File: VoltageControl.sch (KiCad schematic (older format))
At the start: 7 parts

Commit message: Annotated sheets
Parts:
- gave numbers to parts that had none: 7
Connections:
- net at R201.1, RV201.3: now also U201.3 (+); no longer U201.5 (+)
- net at R202.2, R203.1: now also U201.2 (-); no longer U201.6 (-)
- net at D201.1 (K): now also U201.1; no longer U201.7
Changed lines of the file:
@@
 $EndDescr
 $Comp
-L LMV358 U?
-U 2 1 56A5F69C
+L LMV358 U201
+U 1 1 56A5F69C
 P 4250 4800
-F 0 "U?" H 4200 5000 60  0000 L CNN
+F 0 "U201" H 4200 5000 60  0000 L CNN
 F 1 "LMV358" H 4200 4550 60  0000 L CNN
 F 2 "" H 4250 4800 60  0000 C CNN
 F 3 "" H 4250 4800 60  0000 C CNN
-	2    4250 4800
+	1    4250 4800
 	1    0    0    -1
 $EndComp
 $Comp
-L R R?
+L R R201
 U 1 1 56A5F6A3
 P 2250 5750
-F 0 "R?" V 2330 5750 50  0000 C CNN
+F 0 "R201" V 2330 5750 50  0000 C CNN
 F 1 "R" V 2250 5750 50  0000 C CNN
 F 2 "" V 2180 5750 50  0000 C CNN
@@
 $EndComp
 $Comp
-L GND #PWR?
+L GND #PWR202
 U 1 1 56A5F6AA
 P 4150 5300
-F 0 "#PWR?" H 4150 5050 50  0001 C CNN
+F 0 "#PWR202" H 4150 5050 50  0001 C CNN
 F 1 "GND" H 4150 5150 50  0000 C CNN
 F 2 "" H 4150 5300 60  0000 C CNN
@@
 $EndComp
 $Comp
-L POT RV?
+L POT RV201
 U 1 1 56A5F6B0
 P 2250 4950
-F 0 "RV?" H 2250 4850 50  0000 C CNN
+F 0 "RV201" H 2250 4850 50  0000 C CNN
 F 1 "POT" H 2250 4950 50  0000 C CNN
 F 2 "" H 2250 4950 50  0000 C CNN
@@
 $EndComp
 $Comp
-L C C?
+L C C201
 U 1 1 56A5F6B7
 P 3450 4100
-F 0 "C?" H 3475 4200 50  0000 L CNN
+F 0 "C201" H 3475 4200 50  0000 L CNN
 F 1 "C" H 3475 4000 50  0000 L CNN
 F 2 "" H 3488 3950 50  0000 C CNN
@@
 $EndComp
 $Comp
-L GND #PWR?
+L GND #PWR201
 U 1 1 56A5F6BE
 P 3450 4400
-F 0 "#PWR?" H 3450 4150 50  0001 C CNN
+F 0 "#PWR201" H 3450 4150 50  0001 C CNN
 F 1 "GND" H 3450 4250 50  0000 C CNN
 F 2 "" H 3450 4400 50  0000 C CNN
@@
 	4750 4800 5000 4800
 $Comp
-L D D?
+L D D201
 U 1 1 56A5F700
 P 5150 4800
-F 0 "D?" H 5150 4900 50  0000 C CNN
+F 0 "D201" H 5150 4900 50  0000 C CNN
 F 1 "D" H 5150 4700 50  0000 C CNN
 F 2 "" H 5150 4800 50  0000 C CNN
@@
 $EndComp
 $Comp
-L R R?
+L R R202
 U 1 1 56A5F806
 P 6400 5200
-F 0 "R?" V 6480 5200 50  0000 C CNN
+F 0 "R202" V 6480 5200 50  0000 C CNN
 F 1 "9K" V 6400 5200 50  0000 C CNN
 F 2 "" V 6330 5200 50  0000 C CNN
@@
 $EndComp
 $Comp
-L R R?
+L R R203
 U 1 1 56A5F8A9
 P 6400 5800
-F 0 "R?" V 6480 5800 50  0000 C CNN
+F 0 "R203" V 6480 5800 50  0000 C CNN
 F 1 "1K" V 6400 5800 50  0000 C CNN
 F 2 "" V 6330 5800 50  0000 C CNN

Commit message: Updated BOM
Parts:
- C201: footprint (none) -> Capacitors_SMD:C_0805_HandSoldering
- D201: value D -> 1N4148; footprint (none) -> Diodes_SMD:SOD-123; MPN (none) -> 1N4148WT-7
- R201: value R -> 28.7K; footprint (none) -> Resistors_SMD:R_0805_HandSoldering; MPN (none) -> Value
- R202, R203: footprint (none) -> Resistors_SMD:R_0805_HandSoldering
- RV201: value POT -> 10K; footprint (none) -> current:P090L-02F25BR10K; symbol POT -> POT-RESCUE-CurrentSinkOrSwim
- U201: footprint (none) -> SMD_Packages:SOIC-8-N; MPN (none) -> LMV358IDT
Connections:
- net 2.7V: now also R201.1; no longer RV201.2
- net Current_Sink-: now also RV201.3; no longer R201.2
- new net: R201.2, RV201.2, U201.3 (+)
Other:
- note added: "0-20V"
- note added: "0-2V"
- moved on the sheet: R201, RV201
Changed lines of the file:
@@
 EESchema Schematic File Version 2
+LIBS:CurrentSinkOrSwim-rescue
 LIBS:power
 LIBS:device
@@
 F 0 "U201" H 4200 5000 60  0000 L CNN
 F 1 "LMV358" H 4200 4550 60  0000 L CNN
-F 2 "" H 4250 4800 60  0000 C CNN
+F 2 "SMD_Packages:SOIC-8-N" H 4250 4800 60  0001 C CNN
 F 3 "" H 4250 4800 60  0000 C CNN
+F 4 "LMV358IDT" H 4250 4800 60  0001 C CNN "MPN"
 	1    4250 4800
 	1    0    0    -1
@@
 L R R201
 U 1 1 56A5F6A3
-P 2250 5750
-F 0 "R201" V 2330 5750 50  0000 C CNN
-F 1 "R" V 2250 5750 50  0000 C CNN
-F 2 "" V 2180 5750 50  0000 C CNN
-F 3 "" H 2250 5750 50  0000 C CNN
-	1    2250 5750
-	1    0    0    -1
-$EndComp
-$Comp
-L GND #PWR202
+P 2400 5100
+F 0 "R201" V 2480 5100 50  0000 C CNN
+F 1 "28.7K" V 2400 5100 50  0000 C CNN
+F 2 "Resistors_SMD:R_0805_HandSoldering" V 2330 5100 50  0001 C CNN
+F 3 "" H 2400 5100 50  0000 C CNN
+F 4 "Value" H 2400 5100 60  0001 C CNN "MPN"
+	1    2400 5100
+	1    0    0    -1
+$EndComp
+$Comp
+L GND #PWR03
 U 1 1 56A5F6AA
 P 4150 5300
-F 0 "#PWR202" H 4150 5050 50  0001 C CNN
+F 0 "#PWR03" H 4150 5050 50  0001 C CNN
 F 1 "GND" H 4150 5150 50  0000 C CNN
 F 2 "" H 4150 5300 60  0000 C CNN
@@
 $EndComp
 $Comp
-L POT RV201
+L POT-RESCUE-CurrentSinkOrSwim RV201
 U 1 1 56A5F6B0
-P 2250 4950
-F 0 "RV201" H 2250 4850 50  0000 C CNN
-F 1 "POT" H 2250 4950 50  0000 C CNN
-F 2 "" H 2250 4950 50  0000 C CNN
-F 3 "" H 2250 4950 50  0000 C CNN
-	1    2250 4950
+P 2250 5650
+AR Path="/56A5F6B0" Ref="RV201"  Part="1"
+AR Path="/56A5B830/56A5F6B0" Ref="RV201"  Part="1"
+F 0 "RV201" H 2250 5550 50  0000 C CNN
+F 1 "10K" H 2250 5650 50  0000 C CNN
+F 2 "current:P090L-02F25BR10K" H 2250 5650 50  0001 C CNN
+F 3 "" H 2250 5650 50  0000 C CNN
+	1    2250 5650
 	0    1    1    0
 $EndComp
@@
 F 0 "C201" H 3475 4200 50  0000 L CNN
 F 1 "C" H 3475 4000 50  0000 L CNN
-F 2 "" H 3488 3950 50  0000 C CNN
+F 2 "Capacitors_SMD:C_0805_HandSoldering" H 3488 3950 50  0001 C CNN
 F 3 "" H 3450 4100 50  0000 C CNN
 	1    3450 4100
@@
 $EndComp
 $Comp
-L GND #PWR201
+L GND #PWR04
 U 1 1 56A5F6BE
 P 3450 4400
-F 0 "#PWR201" H 3450 4150 50  0001 C CNN
+F 0 "#PWR04" H 3450 4150 50  0001 C CNN
 F 1 "GND" H 3450 4250 50  0000 C CNN
 F 2 "" H 3450 4400 50  0000 C CNN
@@
 	4150 5300 4150 5200
 Wire Wire Line
-	2250 5200 2250 5600
-Wire Wire Line
-	3550 5550 6400 5550
-Wire Wire Line
 	3550 5550 3550 4900
 Wire Wire Line
@@
 	3750 4700 3100 4700
 Wire Wire Line
-	3100 4700 3100 5350
-Wire Wire Line
-	3100 5350 2250 5350
-Connection ~ 2250 5350
+	3100 4700 3100 5650
 Wire Wire Line
 	2400 3800 4150 3800
@@
 P 5150 4800
 F 0 "D201" H 5150 4900 50  0000 C CNN
-F 1 "D" H 5150 4700 50  0000 C CNN
-F 2 "" H 5150 4800 50  0000 C CNN
+F 1 "1N4148" H 5150 4700 50  0000 C CNN
+F 2 "Diodes_SMD:SOD-123" H 5150 4800 50  0001 C CNN
 F 3 "" H 5150 4800 50  0000 C CNN
+F 4 "1N4148WT-7" H 5150 4800 60  0001 C CNN "MPN"
 	1    5150 4800
 	1    0    0    -1
@@
 F 0 "R202" V 6480 5200 50  0000 C CNN
 F 1 "9K" V 6400 5200 50  0000 C CNN
-F 2 "" V 6330 5200 50  0000 C CNN
+F 2 "Resistors_SMD:R_0805_HandSoldering" V 6330 5200 50  0001 C CNN
 F 3 "" H 6400 5200 50  0000 C CNN
 	1    6400 5200
@@
 F 0 "R203" V 6480 5800 50  0000 C CNN
 F 1 "1K" V 6400 5800 50  0000 C CNN
-F 2 "" V 6330 5800 50  0000 C CNN
+F 2 "Resistors_SMD:R_0805_HandSoldering" V 6330 5800 50  0001 C CNN
 F 3 "" H 6400 5800 50  0000 C CNN
 F 4 "Value" H 6400 5800 60  0001 C CNN "MPN"
@@
 Current_Sink-
 Connection ~ 6400 6250
+Connection ~ 3550 5550
+Wire Wire Line
+	3550 5550 6400 5550
+Wire Wire Line
+	2400 5250 2400 5350
+Wire Wire Line
+	2400 5350 3100 5350
+Connection ~ 3100 5350
+Wire Wire Line
+	3100 5650 2400 5650
+Text Notes 3100 4650 0    60   ~ 0
+0-2V
+Text Notes 5100 5500 0    60   ~ 0
+0-2V
+Text Notes 6550 4950 0    60   ~ 0
+0-20V
 $EndSCHEMATC

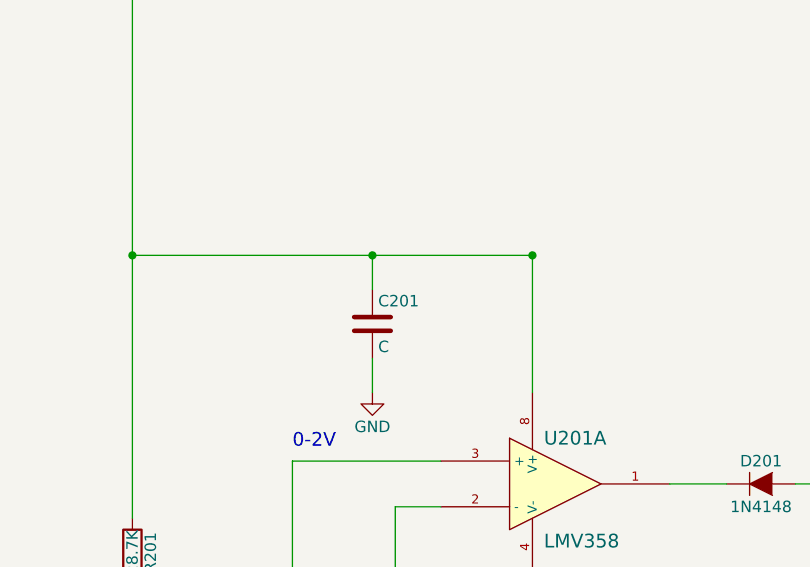
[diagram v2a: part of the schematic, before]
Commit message: This is the version of the file that has been submitted to OSH park
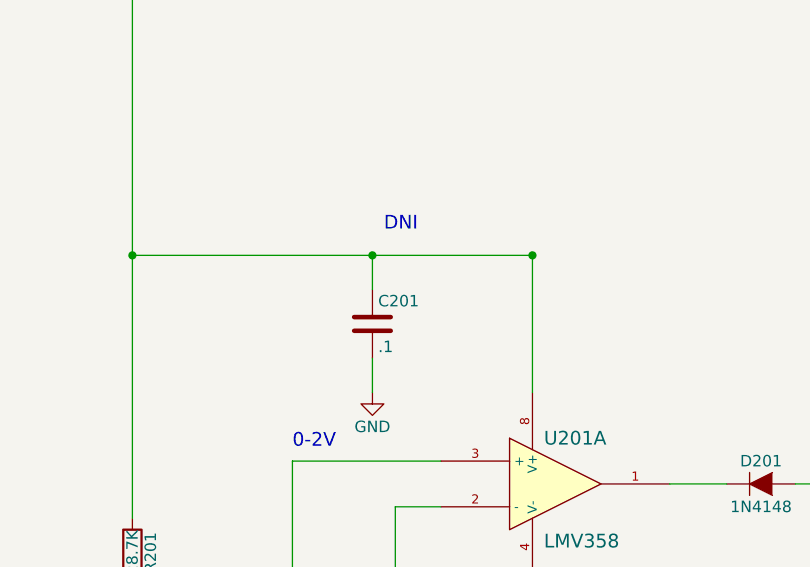
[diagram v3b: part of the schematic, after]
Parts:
- C201: value C -> .1
- RV201: MPN (none) -> P090L-02F25BR10K
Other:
- note added: "DNI"
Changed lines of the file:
@@
 F 2 "current:P090L-02F25BR10K" H 2250 5650 50  0001 C CNN
 F 3 "" H 2250 5650 50  0000 C CNN
+F 4 "P090L-02F25BR10K" H 2250 5650 60  0001 C CNN "MPN"
 	1    2250 5650
 	0    1    1    0
@@
 P 3450 4100
 F 0 "C201" H 3475 4200 50  0000 L CNN
-F 1 "C" H 3475 4000 50  0000 L CNN
+F 1 ".1" H 3475 4000 50  0000 L CNN
 F 2 "Capacitors_SMD:C_0805_HandSoldering" H 3488 3950 50  0001 C CNN
 F 3 "" H 3450 4100 50  0000 C CNN
@@
 Text Notes 6550 4950 0    60   ~ 0
 0-20V
+Text Notes 3500 3700 0    60   ~ 0
+DNI
 $EndSCHEMATC
